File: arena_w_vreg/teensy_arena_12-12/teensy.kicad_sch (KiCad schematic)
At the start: 1 part, among them U13 Teensy4.1

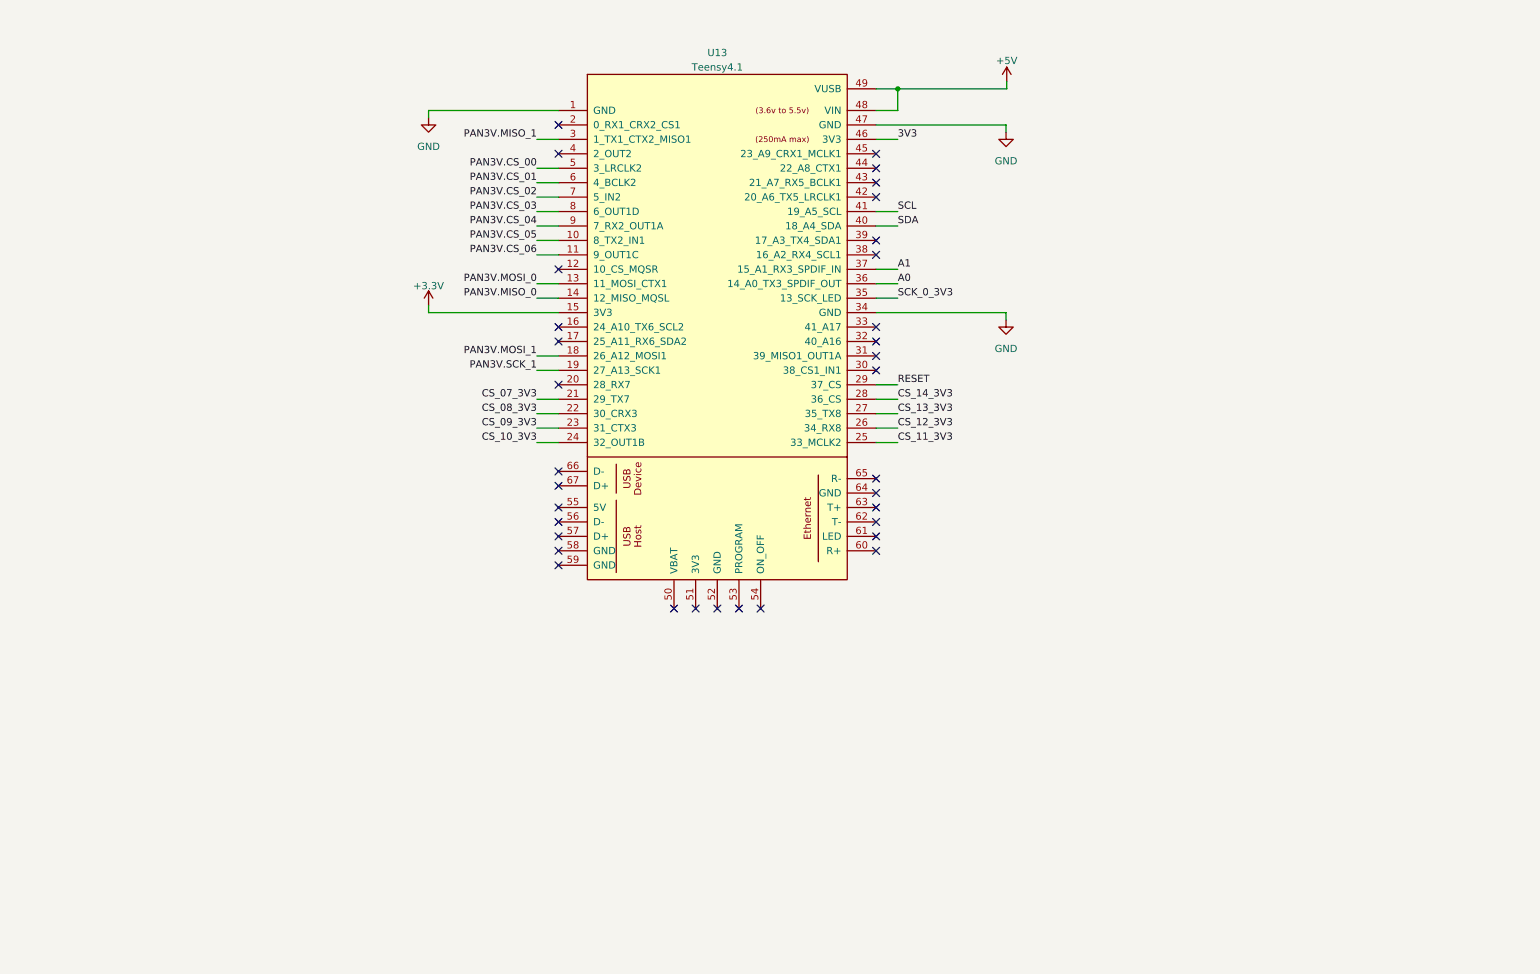
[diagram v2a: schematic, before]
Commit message: Completed initial schematic for 12-12 teensy arena.
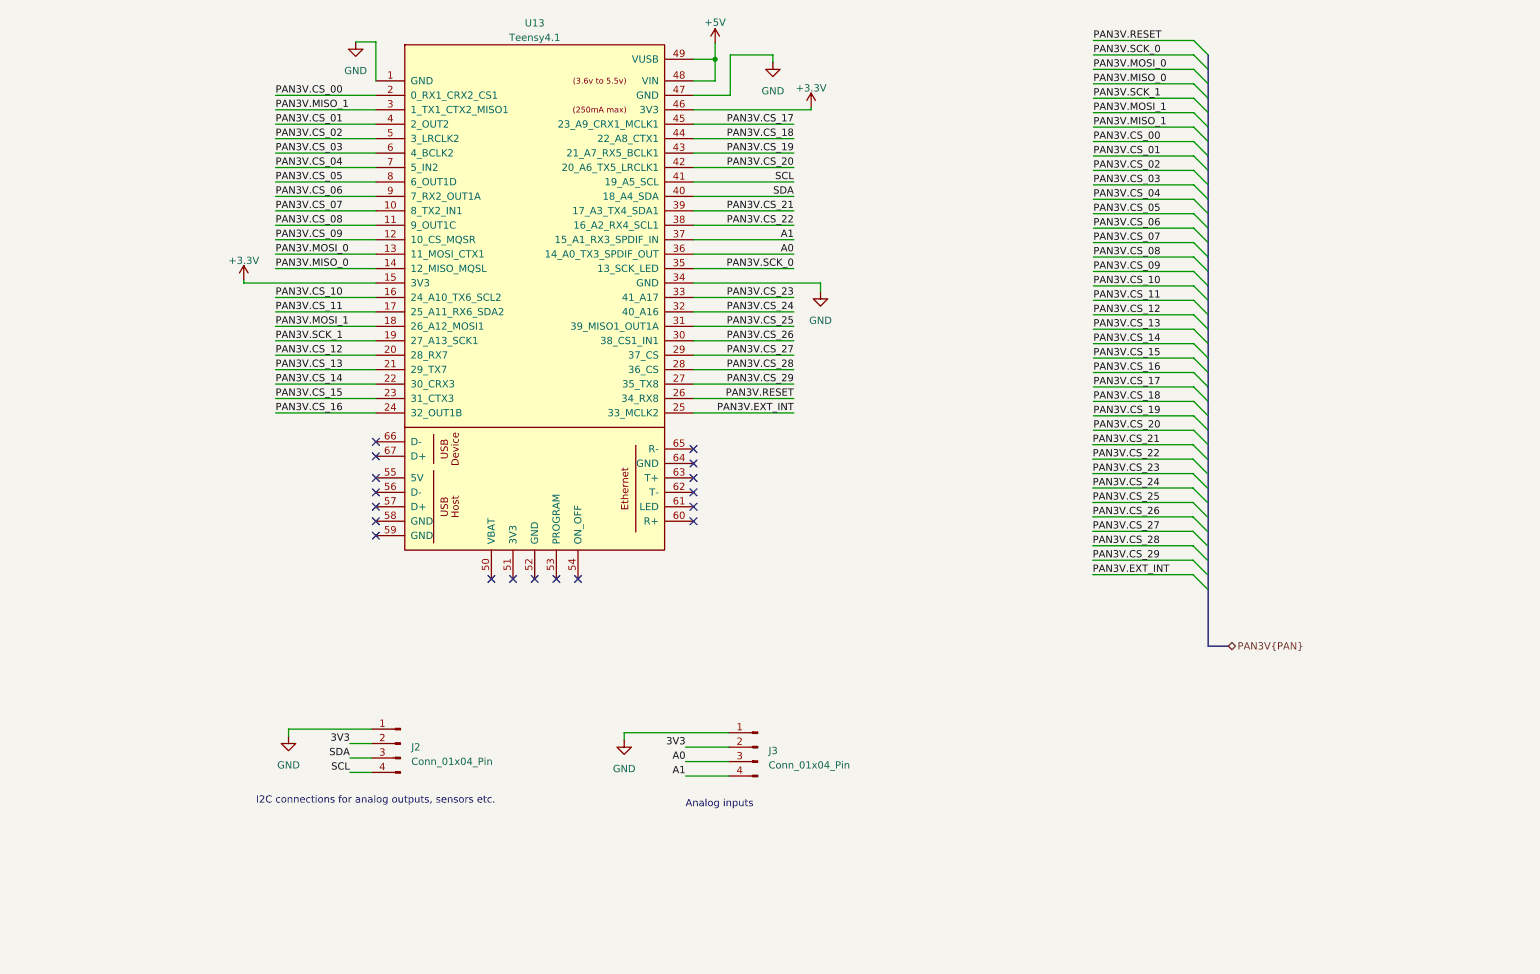
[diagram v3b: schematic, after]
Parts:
- added J2, J3: Conn_01x04_Pin, arena_custom:NS-Tech_Grove_1x04_P2mm_Horizontal, symbol Connector:Conn_01x04_Pin
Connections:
- net +3.3V: now also U13.46 (3V3)
- net 3V3: now also J2.2 (Pin_2), J3.2 (Pin_2); no longer U13.46 (3V3)
- net A0: now also J3.3 (Pin_3)
- net A1: now also J3.4 (Pin_4)
- net GND: now also J2.1 (Pin_1), J3.1 (Pin_1)
- net PAN3V.CS_00: now also U13.2 (0_RX1_CRX2_CS1); no longer U13.5 (3_LRCLK2)
- net PAN3V.CS_01: now also U13.4 (2_OUT2); no longer U13.6 (4_BCLK2)
- net PAN3V.CS_02: now also U13.5 (3_LRCLK2); no longer U13.7 (5_IN2)
- net PAN3V.CS_03: now also U13.6 (4_BCLK2); no longer U13.8 (6_OUT1D)
- net PAN3V.CS_04: now also U13.7 (5_IN2); no longer U13.9 (7_RX2_OUT1A)
- net PAN3V.CS_05: now also U13.8 (6_OUT1D); no longer U13.10 (8_TX2_IN1)
- net PAN3V.CS_06: now also U13.9 (7_RX2_OUT1A); no longer U13.11 (9_OUT1C)
- net SCL: now also J2.4 (Pin_4)
- net SDA: now also J2.3 (Pin_3)
- net PAN3V.CS_09: now reaches U13.12 (10_CS_MQSR)
- net PAN3V.CS_10: now reaches U13.16 (24_A10_TX6_SCL2)
- net PAN3V.CS_11: now reaches U13.17 (25_A11_RX6_SDA2)
- net PAN3V.CS_12: now reaches U13.20 (28_RX7)
- net PAN3V.CS_26: now reaches U13.30 (38_CS1_IN1)
- net PAN3V.CS_25: now reaches U13.31 (39_MISO1_OUT1A)
- net PAN3V.CS_24: now reaches U13.32 (40_A16)
- net PAN3V.CS_23: now reaches U13.33 (41_A17)
- net PAN3V.CS_22: now reaches U13.38 (16_A2_RX4_SCL1)
- net PAN3V.CS_21: now reaches U13.39 (17_A3_TX4_SDA1)
- net PAN3V.CS_20: now reaches U13.42 (20_A6_TX5_LRCLK1)
- net PAN3V.CS_19: now reaches U13.43 (21_A7_RX5_BCLK1)
- net PAN3V.CS_18: now reaches U13.44 (22_A8_CTX1)
- net PAN3V.CS_17: now reaches U13.45 (23_A9_CRX1_MCLK1)
- net CS_07_3V3 renamed PAN3V.CS_13
- net CS_08_3V3 renamed PAN3V.CS_14
- net CS_09_3V3 renamed PAN3V.CS_15
- net CS_10_3V3 renamed PAN3V.CS_16
- net CS_11_3V3 renamed PAN3V.EXT_INT
- net CS_12_3V3 renamed PAN3V.RESET
- net CS_13_3V3 renamed PAN3V.CS_29
- net CS_14_3V3 renamed PAN3V.CS_28
- net RESET renamed PAN3V.CS_27
- net SCK_0_3V3 renamed PAN3V.SCK_0
- new net PAN3V.CS_07: U13.10 (8_TX2_IN1)
- new net PAN3V.CS_08: U13.11 (9_OUT1C)
- no-connect marks 34 -> 18
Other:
- note added: "Analog inputs"
- note added: "I2C connections for analog outputs, sensors etc."
- moved on the sheet: U13

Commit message: Wored on teensy arena.
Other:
- note added: "Notes 1. Currently using grove style header Should I move to Stemma QT/Qwiictype header ... Adafruit DAC MCP4728 Or should I put the MCP4728 right on the arena ... 2. Analog inputs - stick with Grove header or use some other type of connector?"
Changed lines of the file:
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@@
     (stroke (width 0) (type default))
+  )
+  (text "Notes\n\n1. Currently using grove style header \n   Should I move to Stemma QT/Qwiictype header ... Adafruit DAC  MCP4728\n   Or should I put the MCP4728 right on the arena ... \n\n2. Analog inputs - stick with Grove header or use some other type of connector? "
+    (at 13.081 187.96 0)
+    (effects (font (size 2.54 2.54)) (justify left bottom))
   )
   (text "Analog inputs" (at 131.699 161.798 0)

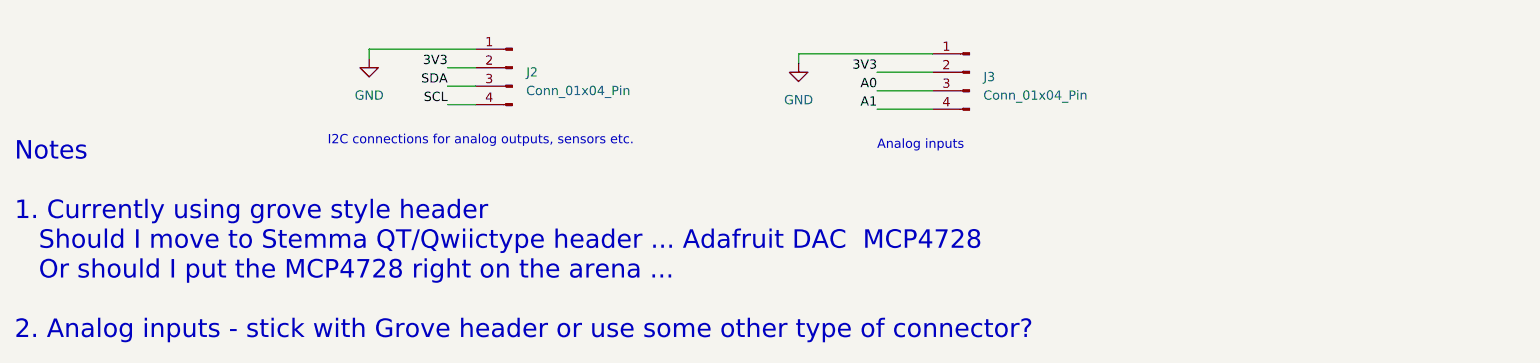
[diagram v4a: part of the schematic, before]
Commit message: Worked on 12-12 schematic & part selection.
Added new 5A regulators. Added load resistors so that regulators
always have minimum load.
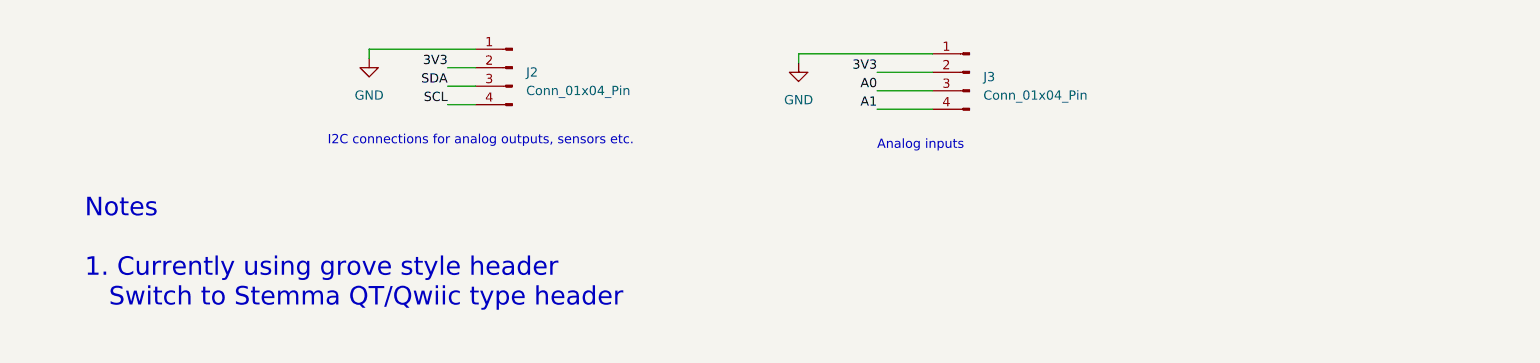
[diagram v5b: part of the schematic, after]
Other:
- note added: "Notes 1. Currently using grove style header Switch to Stemma QT/Qwiic type header"
- note removed: "Notes 1. Currently using grove style header Should I move to Stemma QT/Qwiictype header ... Adafruit DAC MCP4728 Or should I put the MCP4728 right on the arena ... 2. Analog inputs - stick with Grove header or use some other type of connector?"
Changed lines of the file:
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@@
     (stroke (width 0) (type default))
   )
-  (text "Notes\n\n1. Currently using grove style header \n   Should I move to Stemma QT/Qwiictype header ... Adafruit DAC  MCP4728\n   Or should I put the MCP4728 right on the arena ... \n\n2. Analog inputs - stick with Grove header or use some other type of connector? "
-    (at 13.081 187.96 0)
+  (text "Notes\n\n1. Currently using grove style header \n   Switch to Stemma QT/Qwiic type header  \n\n"
+    (at 22.733 187.579 0)
     (effects (font (size 2.54 2.54)) (justify left bottom))
   )

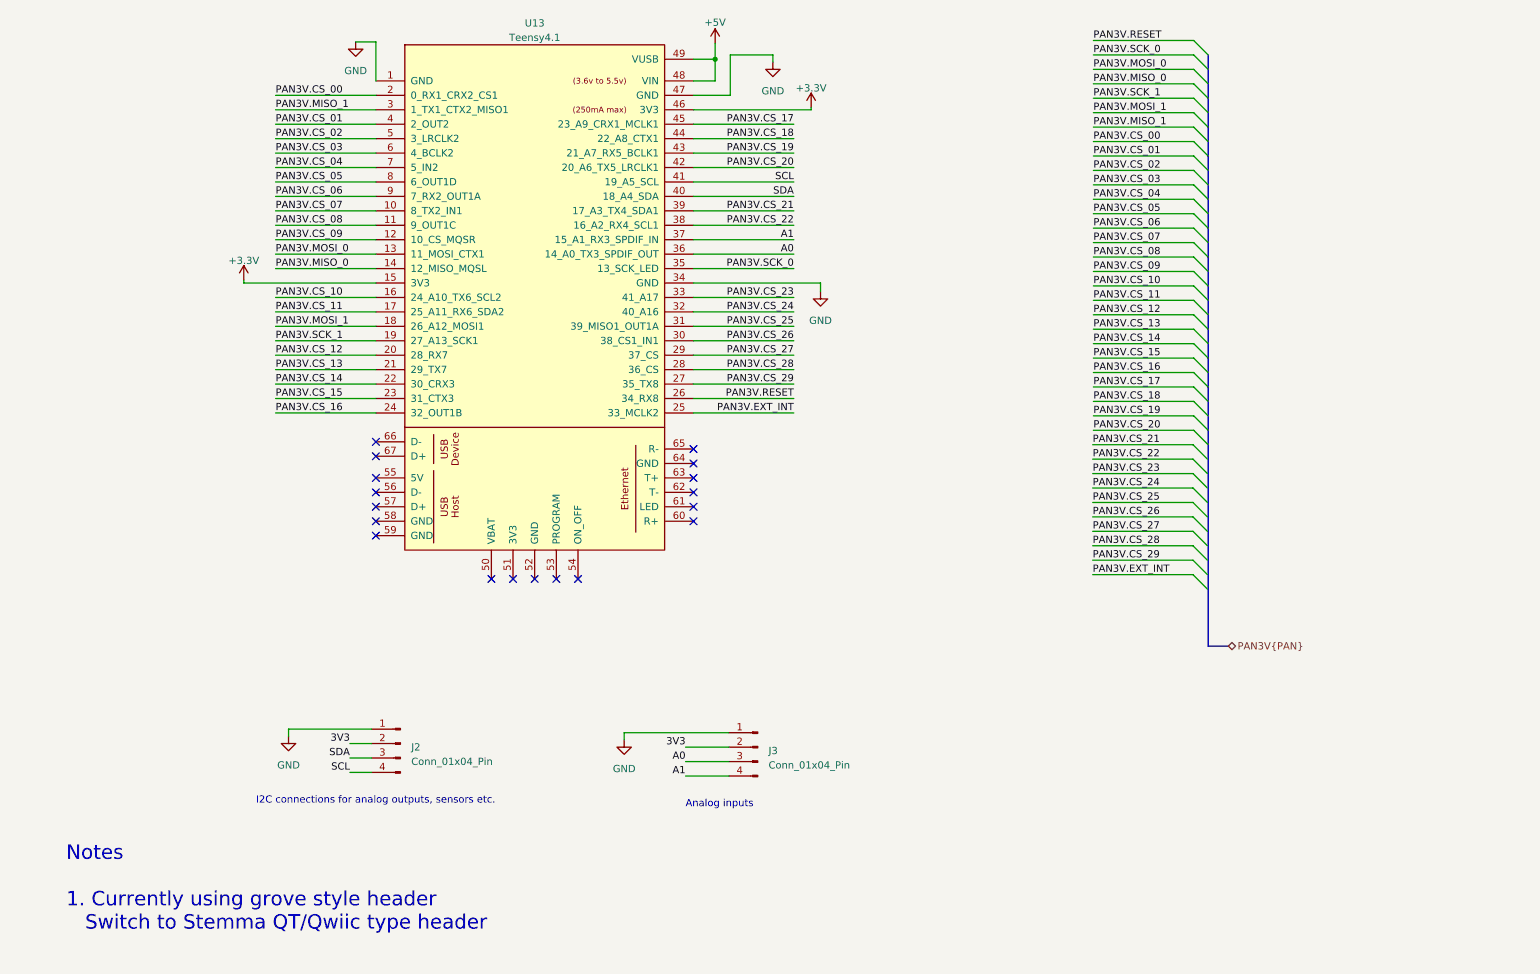
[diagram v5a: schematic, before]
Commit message: Finished footprint assignment. Added notes. Modified header footprint.
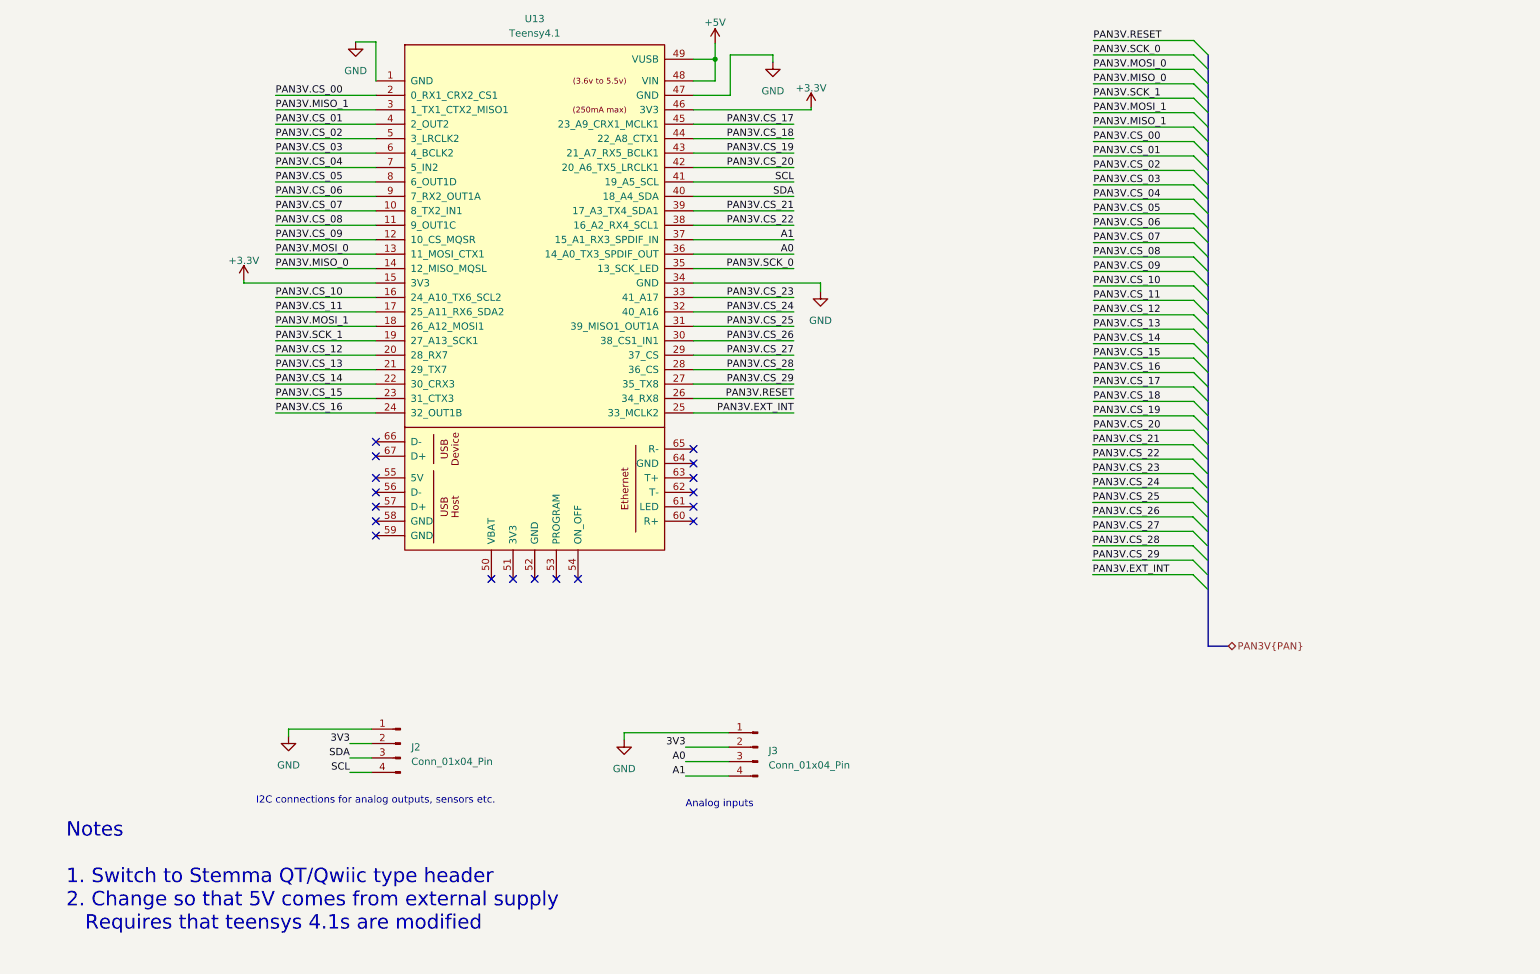
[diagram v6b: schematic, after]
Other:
- note added: "Notes 1. Switch to Stemma QT/Qwiic type header 2. Change so that 5V comes from external supply Requires that teensys 4.1s are modified"
- note removed: "Notes 1. Currently using grove style header Switch to Stemma QT/Qwiic type header"
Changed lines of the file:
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@@
     (stroke (width 0) (type default))
   )
-  (text "Notes\n\n1. Currently using grove style header \n   Switch to Stemma QT/Qwiic type header  \n\n"
+  (text "Notes\n\n1. Switch to Stemma QT/Qwiic type header  \n2. Change so that 5V comes from external supply \n   Requires that teensys 4.1s are modified\n\n"
     (at 22.733 187.579 0)
     (effects (font (size 2.54 2.54)) (justify left bottom))
@@
   (symbol (lib_id "arena_custom:Teensy4.1") (at 105.156 88.392 0) (unit 1)
     (in_bom yes) (on_board yes) (dnp no) (fields_autoplaced)
-    (property "Reference" "U13" (at 105.156 23.622 0)
+    (property "Reference" "U13" (at 105.156 22.86 0)
       (effects (font (size 1.27 1.27)))
     )
-    (property "Value" "Teensy4.1" (at 105.156 26.162 0)
+    (property "Value" "Teensy4.1" (at 105.156 25.4 0)
       (effects (font (size 1.27 1.27)))
     )
@@
         )
         (path "/a2511654-3a17-43f1-8b9e-c45e375533dc/5b6d0be6-08d3-404a-9e9b-565c640343d3"
-          (reference "U13") (unit 1)
+          (reference "U18") (unit 1)
         )
       )
